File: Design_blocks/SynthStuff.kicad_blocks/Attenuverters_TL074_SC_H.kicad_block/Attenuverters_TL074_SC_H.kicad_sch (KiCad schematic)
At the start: 15 parts, among them U1 TL074

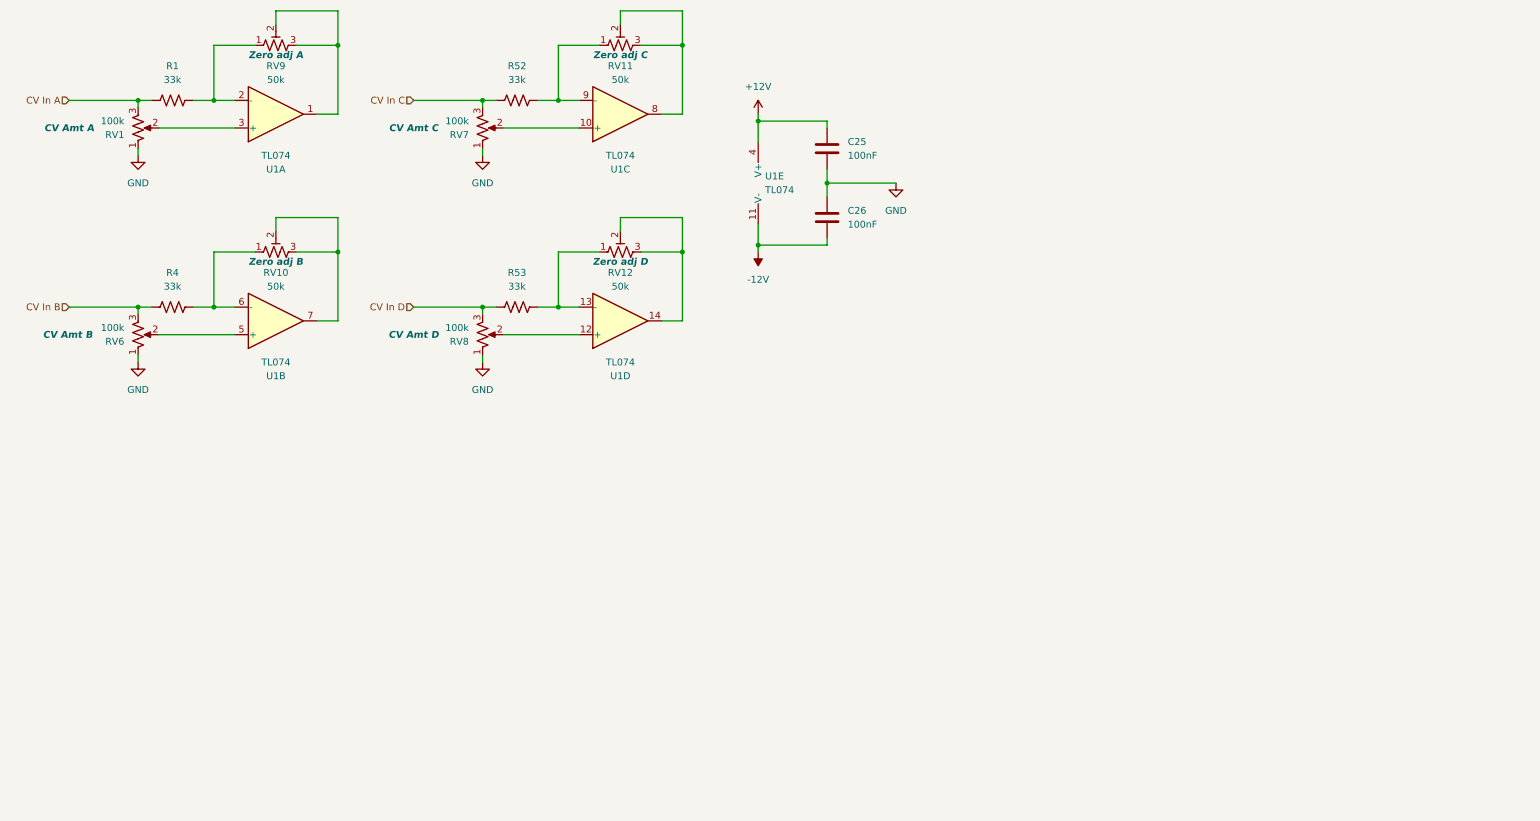
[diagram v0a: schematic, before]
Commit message: Added output label to attenuverter design blocks
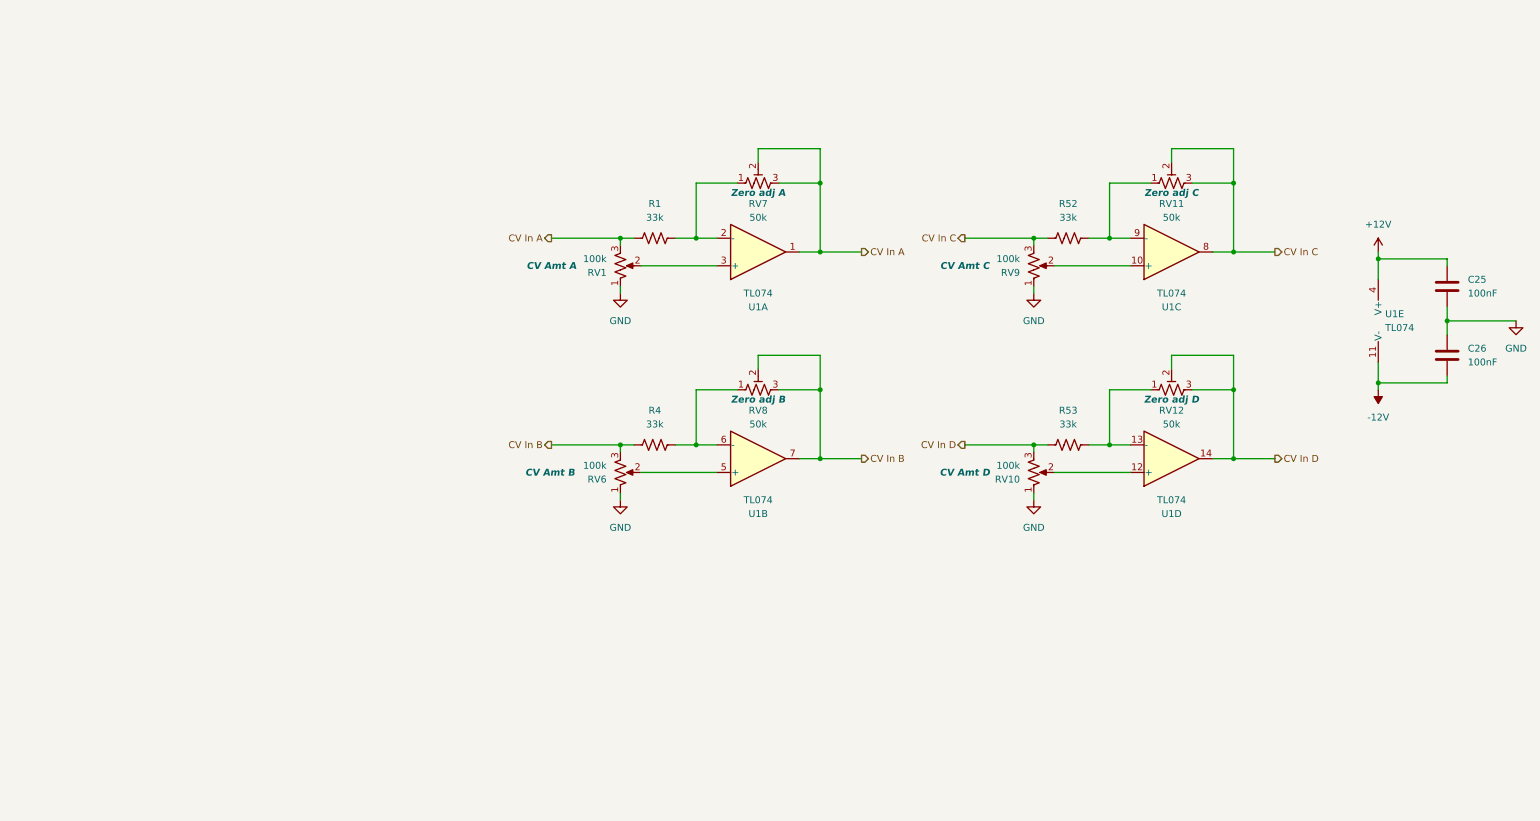
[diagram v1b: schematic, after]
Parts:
- renumbered RV8 to RV10, RV9 to RV7, RV10 to RV8, RV7 to RV9
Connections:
- net CV In A: now also RV7.2, RV7.3, U1.1
- net CV In B: now also RV8.2, RV8.3, U1.7
- net CV In C: now also RV11.2, RV11.3, U1.8
- net CV In D: now also RV12.2, RV12.3, U1.14
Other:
- moved on the sheet: C25, C26, R1, R4, R52, R53, RV1, RV10, RV11, RV12, RV6, RV7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

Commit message: Corrected attenuverter design block output labels
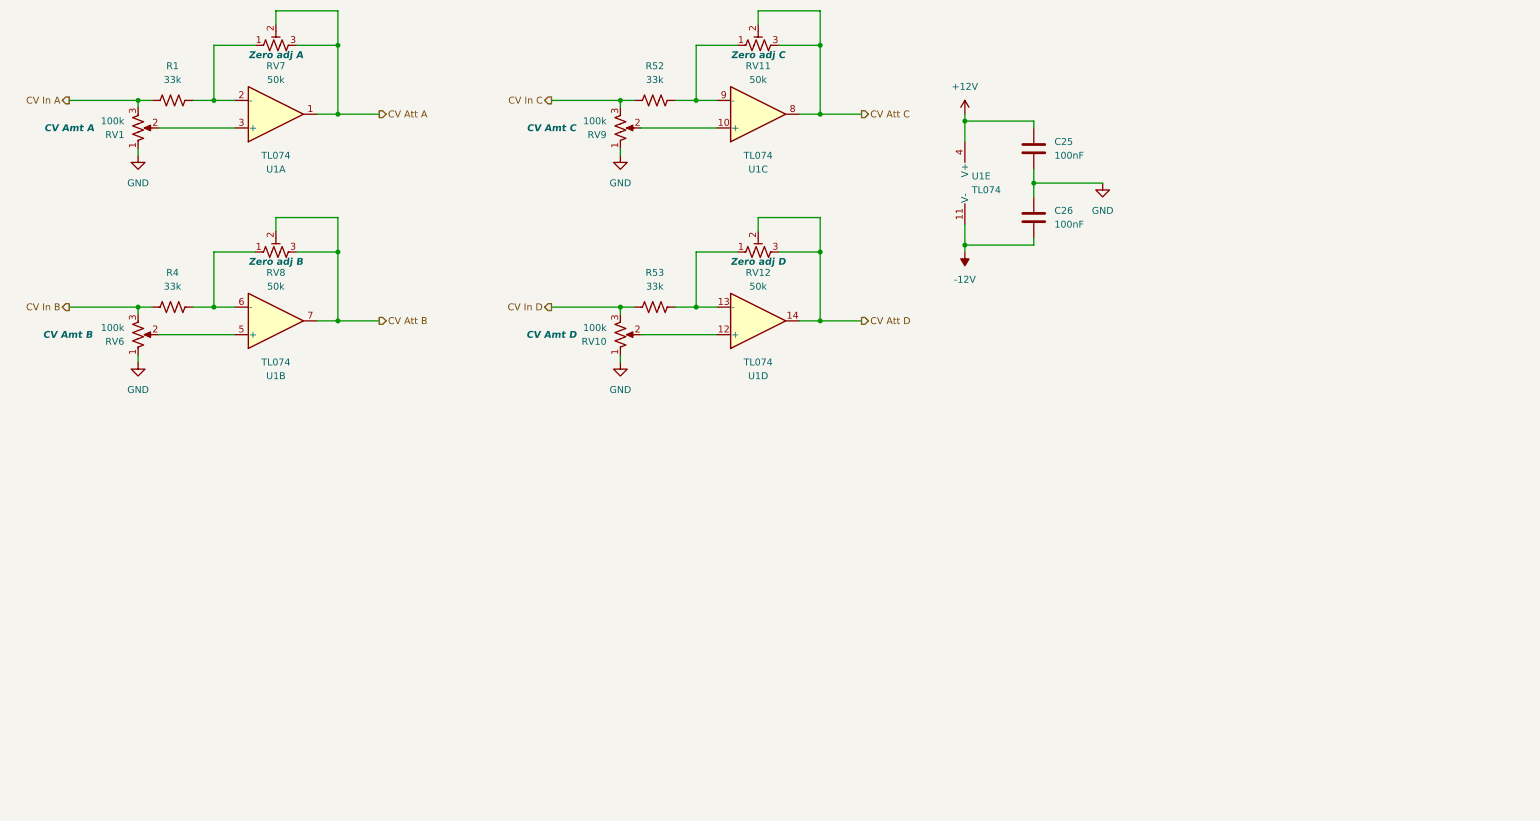
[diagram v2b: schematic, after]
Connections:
- net CV In A: no longer RV7.2, RV7.3, U1.1
- net CV In B: no longer RV8.2, RV8.3, U1.7
- net CV In C: no longer RV11.2, RV11.3, U1.8
- net CV In D: no longer RV12.2, RV12.3, U1.14
- new net CV Att A: RV7.2, RV7.3, U1.1
- new net CV Att B: RV8.2, RV8.3, U1.7
- new net CV Att C: RV11.2, RV11.3, U1.8
- new net CV Att D: RV12.2, RV12.3, U1.14
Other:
- moved on the sheet: C25, C26, R1, R4, R52, R53, RV1, RV10, RV11, RV12, RV6, RV7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

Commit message: Update Attenuverters_TL074_SC_H.kicad_sch
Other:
- moved on the sheet: C25, C26, R1, RV1, RV10, RV12, RV7, RV9, U1A
